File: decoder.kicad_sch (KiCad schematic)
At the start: 35 parts, among them U1 SAA7114H, X1 ACHL-24.576MHZ-EK

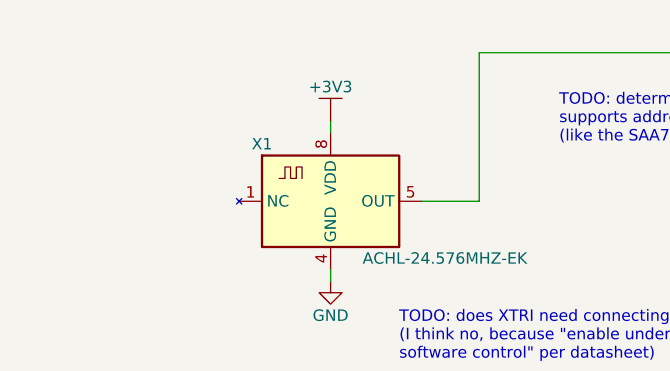
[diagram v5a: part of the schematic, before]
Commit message: footprints and 3d models for caps, connectors
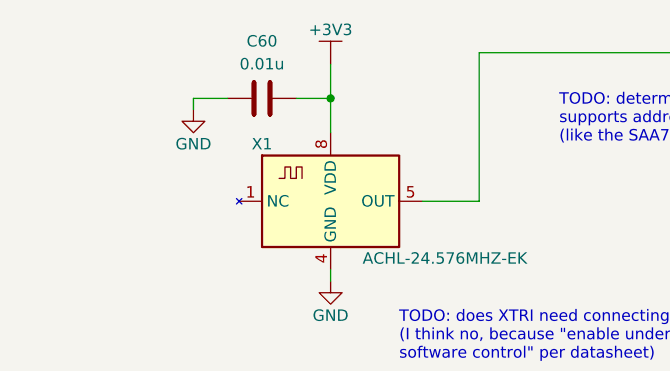
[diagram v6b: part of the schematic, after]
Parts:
- added C60: 0.01u, tbc:C0603, symbol tbc:GCM188R71H103KA37J
- C10, C11, C12, C13, C14, C15, C16, C17, C18, C19, C2, C20, C21, C3, C4, C5, C59, C6, C7, C8, C9: footprint (none) -> tbc:C0603
- X1: footprint (none) -> tbc:ACHL
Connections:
- net +3V3: now also C60.2
- net GND: now also C60.1
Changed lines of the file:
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@@
   (junction (at 140.97 182.88) (diameter 0) (color 0 0 0 0)
+  )
+  (junction (at 49.53 24.13) (diameter 0) (color 0 0 0 0)
   )
   (junction (at 132.08 182.88) (diameter 0) (color 0 0 0 0)
@@
     (stroke (width 0) (type default))
   )
+  (wire (pts (xy 38.1 24.13) (xy 34.29 24.13))
+    (stroke (width 0) (type default))
+  )
+  (wire (pts (xy 49.53 24.13) (xy 49.53 27.94))
+    (stroke (width 0) (type default))
+  )
   (wire (pts (xy 59.69 35.56) (xy 66.04 35.56))
     (stroke (width 0) (type default))
   )
-  (wire (pts (xy 49.53 26.67) (xy 49.53 27.94))
+  (wire (pts (xy 49.53 20.32) (xy 49.53 24.13))
     (stroke (width 0) (type default))
   )
@@
     (stroke (width 0) (type default))
   )
+  (wire (pts (xy 34.29 24.13) (xy 34.29 25.4))
+    (stroke (width 0) (type default))
+  )
   (wire (pts (xy 125.73 19.05) (xy 125.73 30.48))
     (stroke (width 0) (type default))
@@
   )
   (wire (pts (xy 208.28 99.06) (xy 214.63 99.06))
+    (stroke (width 0) (type default))
+  )
+  (wire (pts (xy 45.72 24.13) (xy 49.53 24.13))
     (stroke (width 0) (type default))
   )
@@
       (effects (font (size 1.27 1.27)))
     )
-    (property "Footprint" "" (at 92.71 124.46 0)
+    (property "Footprint" "tbc:C0603" (at 92.71 124.46 0)
       (effects (font (size 1.27 1.27)) hide)
     )
@@
       (effects (font (size 1.27 1.27)) (justify right))
     )
-    (property "Footprint" "" (at 116.84 177.8 0)
+    (property "Footprint" "tbc:C0603" (at 116.84 177.8 0)
       (effects (font (size 1.27 1.27)) hide)
     )
@@
       (effects (font (size 1.27 1.27)))
     )
-    (property "Footprint" "" (at 92.71 118.11 0)
+    (property "Footprint" "tbc:C0603" (at 92.71 118.11 0)
       (effects (font (size 1.27 1.27)) hide)
     )
@@
       (effects (font (size 1.27 1.27)) (justify right))
     )
-    (property "Footprint" "" (at 53.34 177.8 0)
+    (property "Footprint" "tbc:C0603" (at 53.34 177.8 0)
       (effects (font (size 1.27 1.27)) hide)
     )
@@
       (effects (font (size 1.27 1.27)) (justify right))
     )
-    (property "Footprint" "" (at 107.95 177.8 0)
+    (property "Footprint" "tbc:C0603" (at 107.95 177.8 0)
       (effects (font (size 1.27 1.27)) hide)
     )
@@
       (effects (font (size 1.27 1.27)))
     )
-    (property "Footprint" "" (at 92.71 130.81 0)
+    (property "Footprint" "tbc:C0603" (at 92.71 130.81 0)
       (effects (font (size 1.27 1.27)) hide)
     )
@@
       (effects (font (size 1.27 1.27)) (justify right))
     )
-    (property "Footprint" "" (at 179.07 177.8 0)
+    (property "Footprint" "tbc:C0603" (at 179.07 177.8 0)
       (effects (font (size 1.27 1.27)) hide)
     )
@@
       (effects (font (size 1.27 1.27)) (justify right))
     )
-    (property "Footprint" "" (at 71.12 177.8 0)
+    (property "Footprint" "tbc:C0603" (at 71.12 177.8 0)
       (effects (font (size 1.27 1.27)) hide)
     )
@@
       (effects (font (size 1.27 1.27)))
     )
-    (property "Footprint" "" (at 106.68 158.75 0)
+    (property "Footprint" "tbc:C0603" (at 106.68 158.75 0)
       (effects (font (size 1.27 1.27)) hide)
     )
@@
     )
   )
+  (symbol (lib_id "tbc:GND") (at 34.29 25.4 0) (unit 1)
+    (in_bom yes) (on_board yes) (dnp no)
+    (property "Reference" "#PWR065" (at 34.29 31.75 0)
+      (effects (font (size 1.27 1.27)) hide)
+    )
+    (property "Value" "GND" (at 34.29 29.21 0)
+      (effects (font (size 1.27 1.27)))
+    )
+    (property "Footprint" "" (at 34.29 25.4 0)
+      (effects (font (size 1.27 1.27)) hide)
+    )
+    (property "Datasheet" "" (at 34.29 25.4 0)
+      (effects (font (size 1.27 1.27)) hide)
+    )
+    (property "Sim.Enable" "0" (at 34.29 25.4 0)
+      (effects (font (size 1.27 1.27)) hide)
+    )
+    (pin "1")
+    (instances
+      (project "tbc"
+        (path "/9df71e53-7941-4fd3-a17d-93619e4e3e02/23bf4837-f35d-40b3-9230-f145926e4d0d"
+          (reference "#PWR065") (unit 1)
+        )
+      )
+    )
+  )
   (symbol (lib_id "tbc:RC0603FR-0756RL") (at 63.5 130.81 90) (unit 1)
     (in_bom yes) (on_board yes) (dnp no)
@@
       (effects (font (size 1.27 1.27)) (justify right))
     )
-    (property "Footprint" "" (at 90.17 177.8 0)
+    (property "Footprint" "tbc:C0603" (at 90.17 177.8 0)
       (effects (font (size 1.27 1.27)) hide)
     )
@@
       (effects (font (size 1.27 1.27)) (justify right))
     )
-    (property "Footprint" "" (at 99.06 177.8 0)
+    (property "Footprint" "tbc:C0603" (at 99.06 177.8 0)
       (effects (font (size 1.27 1.27)) hide)
     )
@@
       (effects (font (size 1.27 1.27)) (justify right))
     )
-    (property "Footprint" "" (at 134.62 177.8 0)
+    (property "Footprint" "tbc:C0603" (at 134.62 177.8 0)
       (effects (font (size 1.27 1.27)) hide)
     )
@@
       (effects (font (size 1.27 1.27)) (justify right))
     )
-    (property "Footprint" "" (at 143.51 177.8 0)
+    (property "Footprint" "tbc:C0603" (at 143.51 177.8 0)
       (effects (font (size 1.27 1.27)) hide)
     )
@@
       (effects (font (size 1.27 1.27)) (justify right))
     )
-    (property "Footprint" "" (at 170.18 177.8 0)
+    (property "Footprint" "tbc:C0603" (at 170.18 177.8 0)
       (effects (font (size 1.27 1.27)) hide)
     )
@@
       (effects (font (size 1.27 1.27)) (justify right))
     )
-    (property "Footprint" "" (at 152.4 177.8 0)
+    (property "Footprint" "tbc:C0603" (at 152.4 177.8 0)
       (effects (font (size 1.27 1.27)) hide)
     )
@@
       (effects (font (size 1.27 1.27)) (justify right))
     )
-    (property "Footprint" "" (at 161.29 177.8 0)
+    (property "Footprint" "tbc:C0603" (at 161.29 177.8 0)
       (effects (font (size 1.27 1.27)) hide)
     )
@@
     )
   )
+  (symbol (lib_id "tbc:GCM188R71H103KA37J") (at 41.91 24.13 0) (unit 1)
+    (in_bom yes) (on_board yes) (dnp no) (fields_autoplaced)
+    (property "Reference" "C60" (at 41.91 17.78 0)
+      (effects (font (size 1.27 1.27)))
+    )
+    (property "Value" "0.01u" (at 41.91 20.32 0)
+      (effects (font (size 1.27 1.27)))
+    )
+    (property "Footprint" "tbc:C0603" (at 41.91 41.91 0) (show_name)
+      (effects (font (size 1.27 1.27)) hide)
+    )
+    (property "Datasheet" "https://au.mouser.com/datasheet/2/281/1/GCM188R71H103KA37_01C-3144181.pdf" (at 27.94 36.83 0) (show_name)
+      (effects (font (size 1.27 1.27)) (justify left) hide)
+    )
+    (property "Mouser" " 81-GCM188R71H103KA7J" (at 27.94 34.29 0) (show_name)
+      (effects (font (size 1.27 1.27)) (justify left) hide)
+    )
+    (property "Sim.Enable" "0" (at 41.91 39.37 0) (show_name)
+      (effects (font (size 1.27 1.27)) hide)
+    )
+    (pin "2")
+    (pin "1")
+    (instances
+      (project "tbc"
+        (path "/9df71e53-7941-4fd3-a17d-93619e4e3e02/23bf4837-f35d-40b3-9230-f145926e4d0d"
+          (reference "C60") (unit 1)
+        )
+      )
+    )
+  )
   (symbol (lib_id "tbc:GCJ188R71H104KA12D") (at 50.8 177.8 90) (unit 1)
     (in_bom yes) (on_board yes) (dnp no)
@@
       (effects (font (size 1.27 1.27)) (justify right))
     )
-    (property "Footprint" "" (at 62.23 177.8 0)
+    (property "Footprint" "tbc:C0603" (at 62.23 177.8 0)
       (effects (font (size 1.27 1.27)) hide)
     )
@@
       (effects (font (size 1.27 1.27)))
     )
-    (property "Footprint" "" (at 92.71 111.76 0)
+    (property "Footprint" "tbc:C0603" (at 92.71 111.76 0)
       (effects (font (size 1.27 1.27)) hide)
     )
@@
     )
   )
-  (symbol (lib_id "tbc:+3V3") (at 49.53 26.67 0) (unit 1)
-    (in_bom yes) (on_board yes) (dnp no)
-    (property "Reference" "#PWR066" (at 49.53 36.83 0)
-      (effects (font (size 1.27 1.27)) hide)
-    )
-    (property "Value" "+3V3" (at 49.53 22.86 0)
-      (effects (font (size 1.27 1.27)))
-    )
-    (property "Footprint" "" (at 49.53 26.67 0)
-      (effects (font (size 1.27 1.27)) hide)
-    )
-    (property "Datasheet" "" (at 49.53 26.67 0)
-      (effects (font (size 1.27 1.27)) hide)
-    )
-    (property "Sim.Enable" "0" (at 49.53 26.67 0)
+  (symbol (lib_id "tbc:+3V3") (at 49.53 20.32 0) (unit 1)
+    (in_bom yes) (on_board yes) (dnp no)
+    (property "Reference" "#PWR066" (at 49.53 30.48 0)
+      (effects (font (size 1.27 1.27)) hide)
+    )
+    (property "Value" "+3V3" (at 49.53 16.51 0)
+      (effects (font (size 1.27 1.27)))
+    )
+    (property "Footprint" "" (at 49.53 20.32 0)
+      (effects (font (size 1.27 1.27)) hide)
+    )
+    (property "Datasheet" "" (at 49.53 20.32 0)
+      (effects (font (size 1.27 1.27)) hide)
+    )
+    (property "Sim.Enable" "0" (at 49.53 20.32 0)
       (effects (font (size 1.27 1.27)) hide)
     )
@@
       (effects (font (size 1.27 1.27)))
     )
-    (property "Footprint" "" (at 52.07 44.45 0)
+    (property "Footprint" "tbc:ACHL" (at 52.07 44.45 0)
       (effects (font (size 1.27 1.27)) hide)
     )
@@
       (effects (font (size 1.27 1.27)))
     )
-    (property "Footprint" "" (at 92.71 137.16 0)
+    (property "Footprint" "tbc:C0603" (at 92.71 137.16 0)
       (effects (font (size 1.27 1.27)) hide)
     )
@@
       (effects (font (size 1.27 1.27)))
     )
-    (property "Footprint" "" (at 92.71 143.51 0)
+    (property "Footprint" "tbc:C0603" (at 92.71 143.51 0)
       (effects (font (size 1.27 1.27)) hide)
     )
@@
       (effects (font (size 1.27 1.27)) (justify right))
     )
-    (property "Footprint" "" (at 125.73 177.8 0)
-      (effects (font (size 1.27 1.27)) hide)
-    )
+    (property "Footprint" "tbc:C0603" (at 125.73 177.8 0)
+      (effects (font (size 1.27 1.27)) hide)
+    )

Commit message: 3V3A component footprints + layout work
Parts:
- C1: footprint (none) -> tbc:GRM32
- L1: footprint (none) -> tbc:DFE201610E
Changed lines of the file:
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@@
       (effects (font (size 1.27 1.27)))
     )
-    (property "Footprint" "" (at 43.18 177.8 0)
+    (property "Footprint" "tbc:GRM32" (at 43.18 177.8 0)
       (effects (font (size 1.27 1.27)) hide)
     )
@@
       (effects (font (size 1.27 1.27)))
     )
-    (property "Footprint" "" (at 22.86 172.72 90)
-      (effects (font (size 1.27 1.27)) hide)
-    )
+    (property "Footprint" "tbc:DFE201610E" (at 22.86 172.72 90)
+      (effects (font (size 1.27 1.27)) hide)
+    )
